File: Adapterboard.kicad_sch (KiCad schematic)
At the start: 72 parts, among them J101 DAC_X, J102 DAC_Y, J103 JTAG, J104 DAC_Z, J105 TUNNEL_IN, J106 Power in +15V, J107 Power in -15V, J108 Power out Preamplifier, J109 Piezo, J110 TUNNEL_1, J111 USB_Connector, U102 DAC X, U103 ESP32-DEVKITC-32D, U104 DAC Y, U106 DAC Z, U107 ADC 8 Click, U108 mint, U109 UniRegensburg, U110 OTH, U201 TL072, U301 TL072

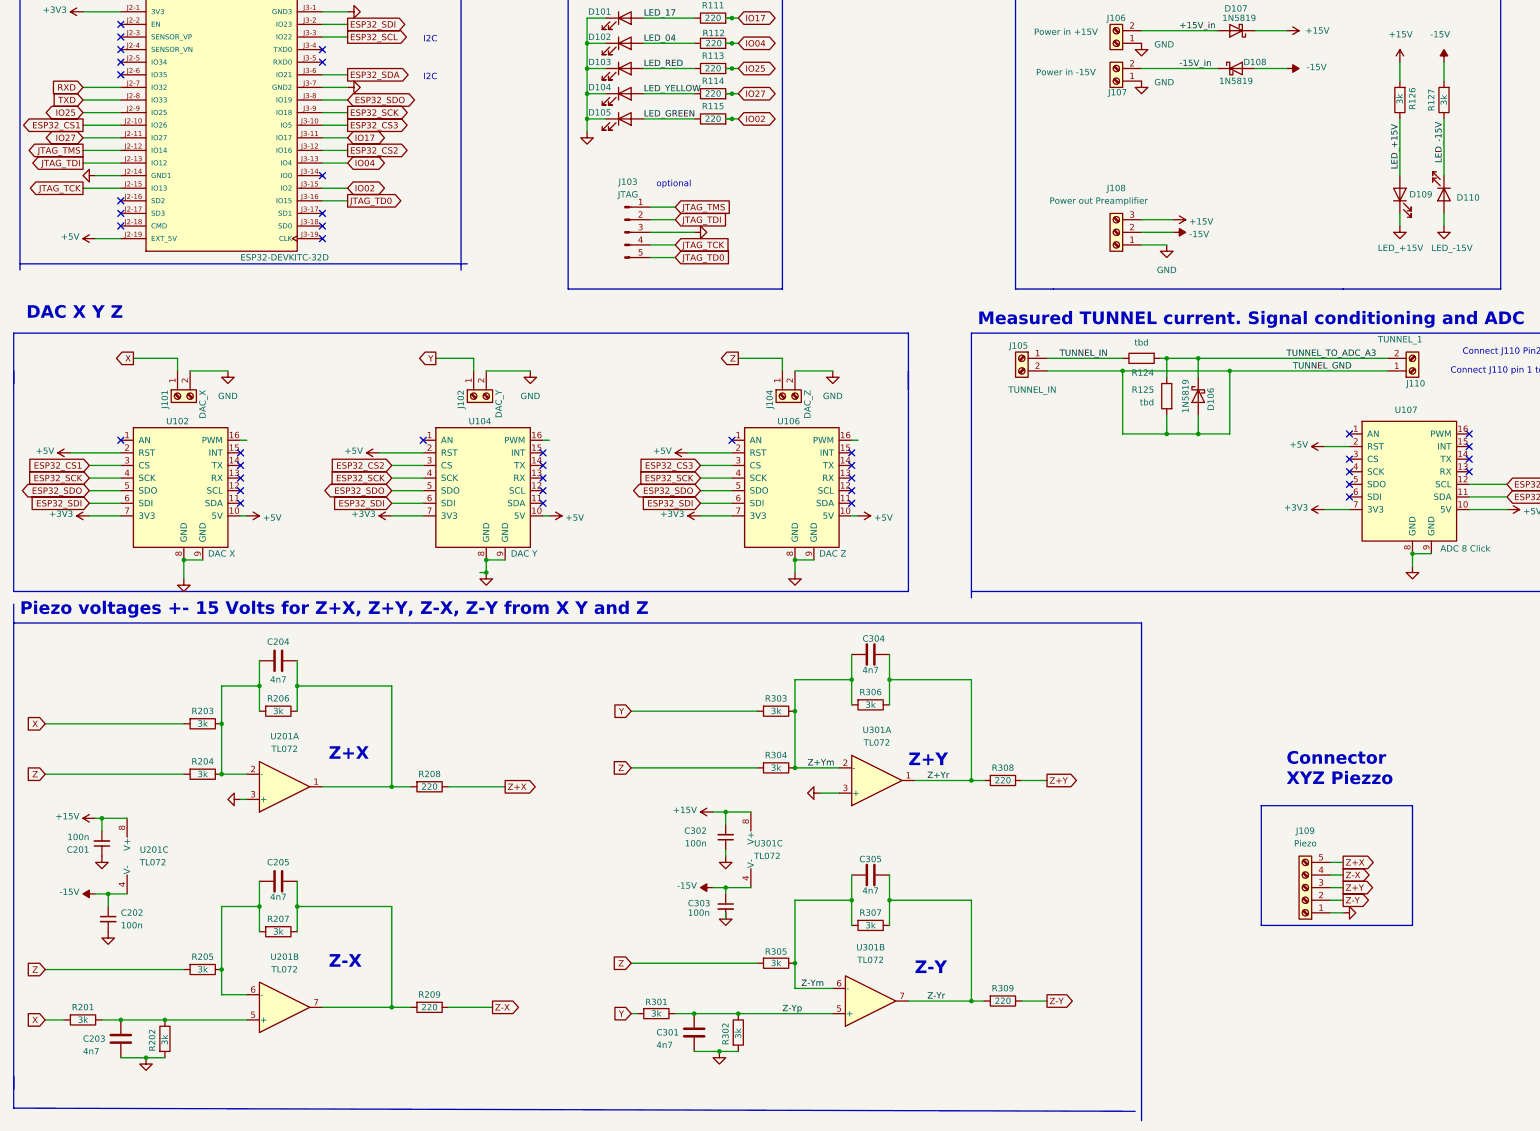
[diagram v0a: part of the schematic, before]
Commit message: pcb ready. add gnd
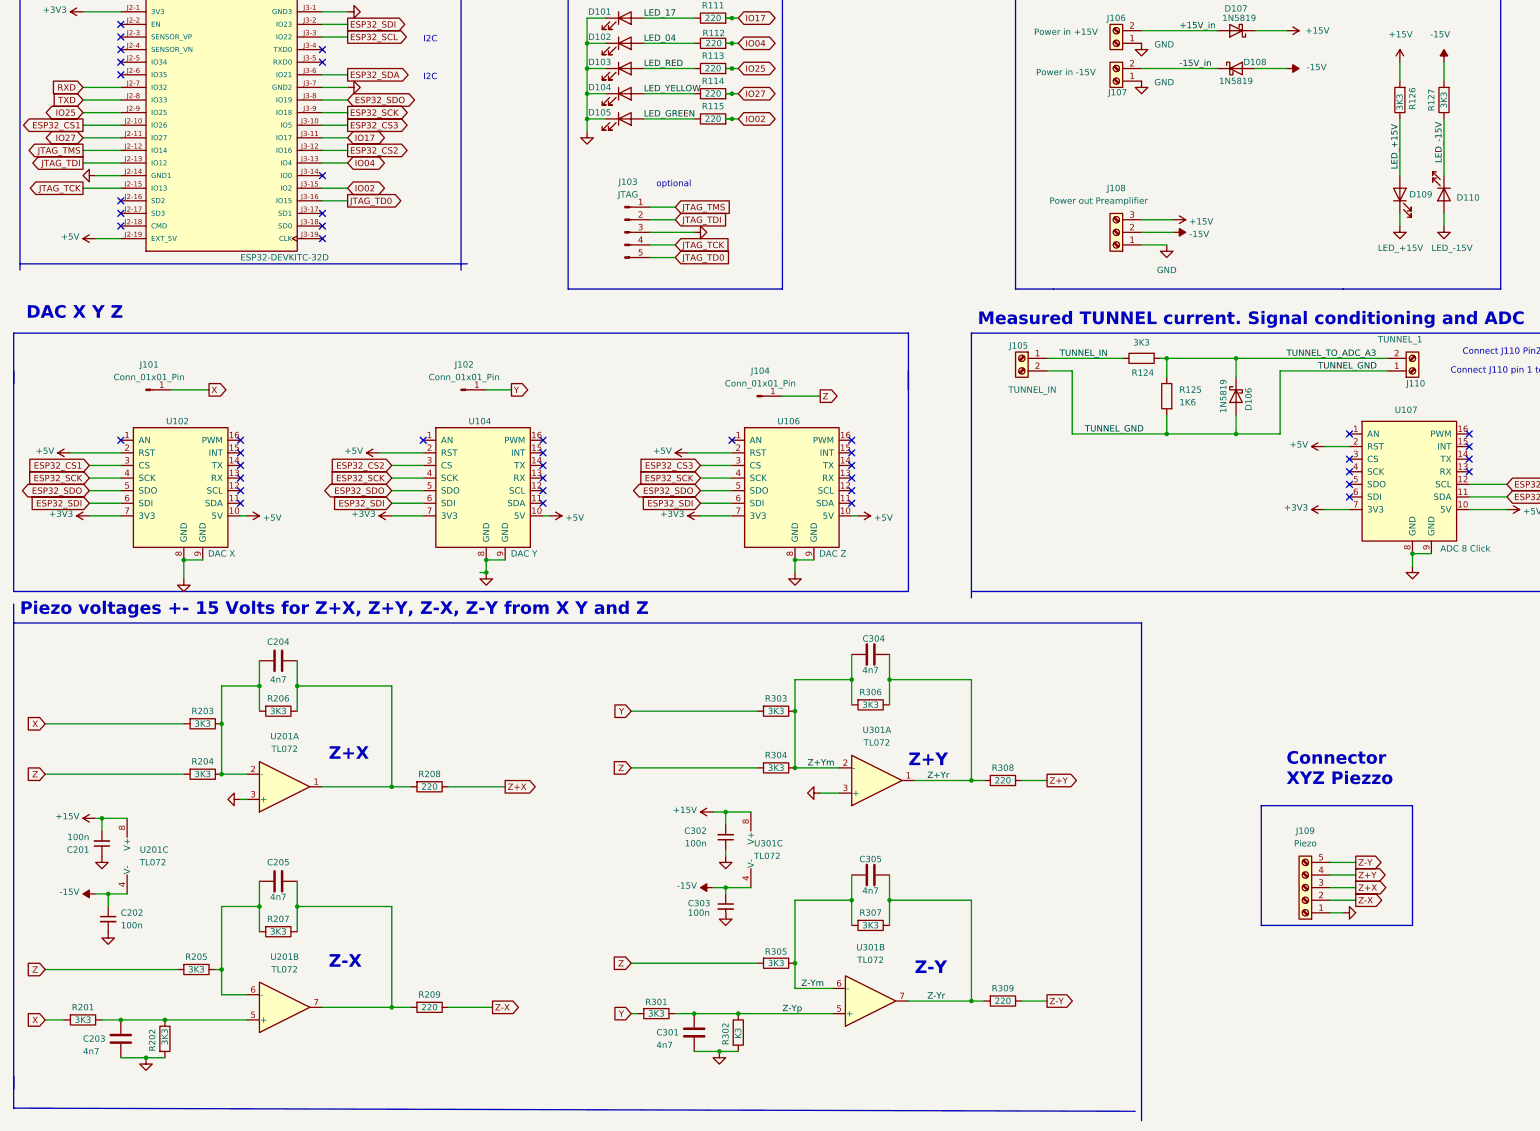
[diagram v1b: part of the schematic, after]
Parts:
- removed J101: DAC_X, TerminalBlock:TerminalBlock_Xinya_XY308-2.54-2P_1x02_P2.54mm_Horizontal, symbol Connector:Screw_Terminal_01x02
- removed J102: DAC_Y, TerminalBlock:TerminalBlock_Xinya_XY308-2.54-2P_1x02_P2.54mm_Horizontal, symbol Connector:Screw_Terminal_01x02
- removed J104: DAC_Z, TerminalBlock:TerminalBlock_Xinya_XY308-2.54-2P_1x02_P2.54mm_Horizontal, symbol Connector:Screw_Terminal_01x02
- added J101, J102, J104: Conn_01x01_Pin, Connector_PinHeader_1.00mm:PinHeader_1x01_P1.00mm_Vertical, symbol Connector:Conn_01x01_Pin
- J110: footprint TerminalBlock:TerminalBlock_Xinya_XY308-2.54-2P_1x02_P2.54mm_Horizontal -> Connector_PinHeader_2.54mm:PinHeader_1x02_P2.54mm_Vertical
- R124: value tbd -> 3K3
- R125: value tbd -> 1K6
- R126, R127, R201, R202, R203, R204, R205, R206, R207, R301, R303, R304, R305, R306, R307: value 3k -> 3K3
- R302: value 3k -> K3
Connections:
- net X: now also J101.1 (Pin_1)
- net Y: now also J102.1 (Pin_1)
- net Z: now also J104.1 (Pin_1)
- net Z+X: now also J109.3 (Pin_3); no longer J109.5 (Pin_5)
- net Z+Y: now also J109.4 (Pin_4); no longer J109.3 (Pin_3)
- net Z-X: now also J109.2 (Pin_2); no longer J109.4 (Pin_4)
- net Z-Y: now also J109.5 (Pin_5); no longer J109.2 (Pin_2)
- no-connect marks 41 -> 44
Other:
- title: 500EUR RTM Adapterboard -> 500EUR STM Adapterboard
- moved on the sheet: D106, R205
